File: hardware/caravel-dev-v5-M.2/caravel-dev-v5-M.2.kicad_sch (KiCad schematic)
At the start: 64 parts, among them J1 USB_B_Micro - 10118193-0001LF, J10 Conn_01x27_Female, J11 Conn_01x20_Female, J2 Conn_01x02_Female, J3 Conn_01x02_Male, J4 Conn_01x04_Female, J5 Conn_01x02_Male, J6 Conn_01x02_Male, J7 Conn_01x06_Female, J8 Conn_01x02_Male, J9 Conn_01x02_Male, SW1 SW_Push - SKQGADE010, T1 Logo, T2 Logo, U1 FT232H, U2 SN74LVC1G125DCKR, U3 SN74LVC1G125DCKR, U4 MCP1319MT-29LE-OT, U5 TAR5SxxU_SOT353F, U6 TAR5SxxU_SOT353F, U7 W25Q32FVSS, U8 caravel-M.2-card, X1 DSC6001_10MHZ, Y1 CSTNE12M0GH5L000R0

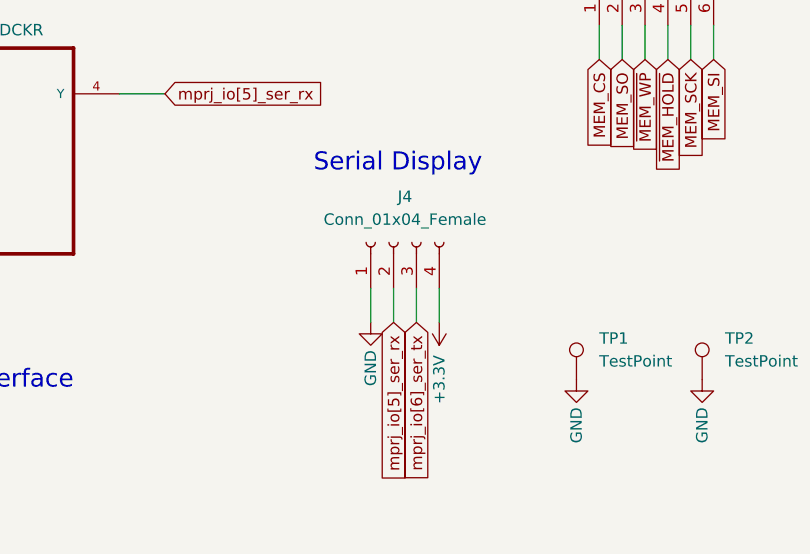
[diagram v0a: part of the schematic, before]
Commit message: rename caravel M.2 carrier board to caravel dev v5 board update Caravel dev (REV5A) pcb:   ~ update the serial display connector to 3-pin   + add large via for the manual reset to be able to monitor it
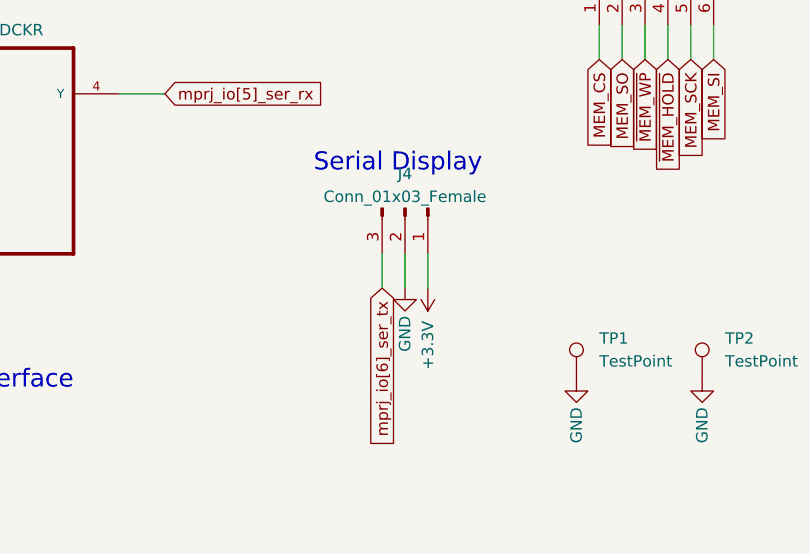
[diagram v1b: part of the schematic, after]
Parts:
- J4: value Conn_01x04_Female -> Conn_01x03_Female; footprint Connector_PinHeader_2.54mm:PinHeader_1x04_P2.54mm_Vertical -> Connector_PinHeader_2.54mm:PinHeader_1x03_P2.54mm_Vertical; symbol Connector:Conn_01x04_Female -> Connector:Conn_01x03_Pin
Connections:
- net +3.3V: now also J4.1 (Pin_1); no longer J4.4 (Pin_4)
- net GND: now also J4.2 (Pin_2); no longer J4.1 (Pin_1)
- net mprj_io[5]_ser_rx: no longer J4.2 (Pin_2)
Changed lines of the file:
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@@
     (stroke (width 0) (type default))
   )
-  (wire (pts (xy 243.84 257.81) (xy 243.84 261.62))
+  (wire (pts (xy 247.65 254) (xy 247.65 257.81))
     (stroke (width 0) (type default))
   )
@@
     (stroke (width 0) (type default))
   )
-  (wire (pts (xy 248.92 257.81) (xy 248.92 261.62))
+  (wire (pts (xy 245.11 254) (xy 245.11 257.81))
     (stroke (width 0) (type default))
   )
@@
     (stroke (width 0) (type default))
   )
-  (wire (pts (xy 251.46 257.81) (xy 251.46 261.62))
+  (wire (pts (xy 250.19 254) (xy 250.19 257.81))
     (stroke (width 0) (type default))
   )
@@
   )
   (wire (pts (xy 54.61 120.65) (xy 54.61 125.73))
-    (stroke (width 0) (type default))
-  )
-  (wire (pts (xy 246.38 257.81) (xy 246.38 261.62))
     (stroke (width 0) (type default))
   )
@@
     )
   )
-  (global_label "mprj_io[5]_ser_rx" (shape input) (at 246.38 261.62 270) (fields_autoplaced)
-    (effects (font (size 1.27 1.27)) (justify right))
-    (property "Intersheetrefs" "${INTERSHEET_REFS}" (at 49.53 574.04 0)
-      (effects (font (size 1.27 1.27)) hide)
-    )
-  )
   (global_label "Caravel_D0" (shape input) (at 327.66 95.25 180) (fields_autoplaced)
     (effects (font (size 1.27 1.27)) (justify right))
@@
     )
   )
-  (global_label "mprj_io[6]_ser_tx" (shape input) (at 248.92 261.62 270) (fields_autoplaced)
-    (effects (font (size 1.27 1.27)) (justify right))
-    (property "Intersheetrefs" "${INTERSHEET_REFS}" (at 49.53 574.04 0)
+  (global_label "mprj_io[6]_ser_tx" (shape input) (at 245.11 257.81 270) (fields_autoplaced)
+    (effects (font (size 1.27 1.27)) (justify right))
+    (property "Intersheetrefs" "${INTERSHEET_REFS}" (at 45.72 570.23 0)
       (effects (font (size 1.27 1.27)) hide)
     )
@@
     )
   )
-  (symbol (lib_id "power:+3.3V") (at 251.46 261.62 180) (unit 1)
+  (symbol (lib_id "power:+3.3V") (at 250.19 257.81 180) (unit 1)
     (in_bom yes) (on_board yes) (dnp no)
-    (property "Reference" "#PWR050" (at 251.46 257.81 0)
-      (effects (font (size 1.27 1.27)) hide)
-    )
-    (property "Value" "+3.3V" (at 251.46 267.97 90)
-      (effects (font (size 1.27 1.27)))
-    )
-    (property "Footprint" "" (at 251.46 261.62 0)
-      (effects (font (size 1.27 1.27)) hide)
-    )
-    (property "Datasheet" "" (at 251.46 261.62 0)
+    (property "Reference" "#PWR050" (at 250.19 254 0)
+      (effects (font (size 1.27 1.27)) hide)
+    )
+    (property "Value" "+3.3V" (at 250.19 264.16 90)
+      (effects (font (size 1.27 1.27)))
+    )
+    (property "Footprint" "" (at 250.19 257.81 0)
+      (effects (font (size 1.27 1.27)) hide)
+    )
+    (property "Datasheet" "" (at 250.19 257.81 0)
       (effects (font (size 1.27 1.27)) hide)
     )
@@
     )
   )
-  (symbol (lib_id "power:GND") (at 243.84 261.62 0) (unit 1)
+  (symbol (lib_id "power:GND") (at 247.65 257.81 0) (unit 1)
     (in_bom yes) (on_board yes) (dnp no)
-    (property "Reference" "#PWR049" (at 243.84 267.97 0)
-      (effects (font (size 1.27 1.27)) hide)
-    )
-    (property "Value" "GND" (at 243.84 266.7 90)
-      (effects (font (size 1.27 1.27)))
-    )
-    (property "Footprint" "" (at 243.84 261.62 0)
-      (effects (font (size 1.27 1.27)) hide)
-    )
-    (property "Datasheet" "" (at 243.84 261.62 0)
+    (property "Reference" "#PWR049" (at 247.65 264.16 0)
+      (effects (font (size 1.27 1.27)) hide)
+    )
+    (property "Value" "GND" (at 247.65 262.89 90)
+      (effects (font (size 1.27 1.27)))
+    )
+    (property "Footprint" "" (at 247.65 257.81 0)
+      (effects (font (size 1.27 1.27)) hide)
+    )
+    (property "Datasheet" "" (at 247.65 257.81 0)
       (effects (font (size 1.27 1.27)) hide)
     )
@@
     )
   )
-  (symbol (lib_id "Connector:Conn_01x04_Female") (at 246.38 252.73 90) (unit 1)
+  (symbol (lib_id "Connector:Conn_01x03_Pin") (at 247.65 248.92 270) (unit 1)
     (in_bom yes) (on_board yes) (dnp no) (fields_autoplaced)
-    (property "Reference" "J4" (at 247.65 247.65 90)
-      (effects (font (size 1.27 1.27)))
-    )
-    (property "Value" "Conn_01x04_Female" (at 247.65 250.19 90)
-      (effects (font (size 1.27 1.27)))
-    )
-    (property "Footprint" "Connector_PinHeader_2.54mm:PinHeader_1x04_P2.54mm_Vertical" (at 246.38 252.73 0)
-      (effects (font (size 1.27 1.27)) hide)
-    )
-    (property "Datasheet" "~" (at 246.38 252.73 0)
+    (property "Reference" "J4" (at 247.65 245.11 90)
+      (effects (font (size 1.27 1.27)))
+    )
+    (property "Value" "Conn_01x03_Female" (at 247.65 247.65 90)
+      (effects (font (size 1.27 1.27)))
+    )
+    (property "Footprint" "Connector_PinHeader_2.54mm:PinHeader_1x03_P2.54mm_Vertical" (at 247.65 248.92 0)
+      (effects (font (size 1.27 1.27)) hide)
+    )
+    (property "Datasheet" "~" (at 247.65 248.92 0)
       (effects (font (size 1.27 1.27)) hide)
     )
@@
     (pin "2")
     (pin "3")
-    (pin "4")
-    (instances
-      (project "caravel-M.2-carrier"
+    (instances
+      (project "caravel-M.2-carrier"
